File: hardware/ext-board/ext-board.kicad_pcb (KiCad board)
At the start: 2 copper layers, 38.5 x 85 mm, 13 parts, among them J1 PTSM 0,5/5-HH-2,5-THR, J2 VCC DATA GND, U1 DS2482-100, U2 DS2482-100 (0x19)

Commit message: hardware: silkscreen tidied, MOV position dropped, copper plots for the review
Plug designators sit below their pin labels (J4's beside the capacitor),
the resistor references run along their bodies, the diode references sit
at the board edge end of each diode, the link header references sit on the
rib strip beside them, the capacitor's beside its lower pad, and the empty
bottom field says why it is empty. The MOV position is gone: the strip
beside the capacitor holds the PTC and the J4 labels, and a clamp on a
class 2 transformer's 24 VAC is a nicety. GPIO8's run from header pin 24
to its breakout pad, which threads the column twice through 0.84 mm gaps,
is laid by hand because the router managed it only sometimes. EXT: C1's
reference moves below the part, clear of the H2 label.

Both boards carry front and back copper plots (back mirrored) from
kicad-cli for checking traces; the review document shows both faces of
each board and the copper.

Co-Authored-By: Claude Fable 5.1 <noreply@anthropic.com>
Claude-Session: https://claude.ai/code/session_01WPMStupqhasFMcGr3goMno
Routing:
- net DATA: track 133.3 -> 158.2 mm, vias 1 -> 0
- net SCL: track 59.8 -> 45.0 mm
- net GND: track 153.7 -> 146.6 mm
- net SDA: track 61.6 -> 56.9 mm
- net H3_DATA: track 37.2 -> 39.0 mm
- net VCC: track 109.1 -> 110.0 mm

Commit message: hardware: EXT link header against the riser field, plug access kept clear
The housing's opening to the INT board, the one the INT link headers sit
beside, falls on the right of the EXT board at the link header's height,
and the PTSM plugs come in and out through it. The power riser is unused
and the housing comes close to the board only at the lower end of its hole
field (David, 2026-09-12), so the riser rule area shrinks to columns 1-3
and J1 moves against it (body x 8.5-22.7), with U2's decoupling beside JP2
and the cleared band marked on the silkscreen.

Routed, DRC clean, schematic parity kept; Gerbers and copper plots
re-exported.

Co-Authored-By: Claude Fable 5.1 <noreply@anthropic.com>
Claude-Session: https://claude.ai/code/session_01WPMStupqhasFMcGr3goMno
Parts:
- moved C2 12.0 mm to (18.5, 34.0)
- moved J1 9.75 mm to (15.6, 44.3)
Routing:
- net VCC: track 110.0 -> 143.0 mm, vias 1 -> 0
- net DATA: track 158.2 -> 143.4 mm
- net SDA: track 56.9 -> 48.7 mm
- net H3_DATA: track 39.0 -> 31.9 mm
- net GPIO4: track 39.6 -> 44.9 mm
- net SCL: track 45.0 -> 50.3 mm, vias 0 -> 1
- net GND: track 146.6 -> 145.5 mm
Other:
- board text added: "plug access: keep clear"

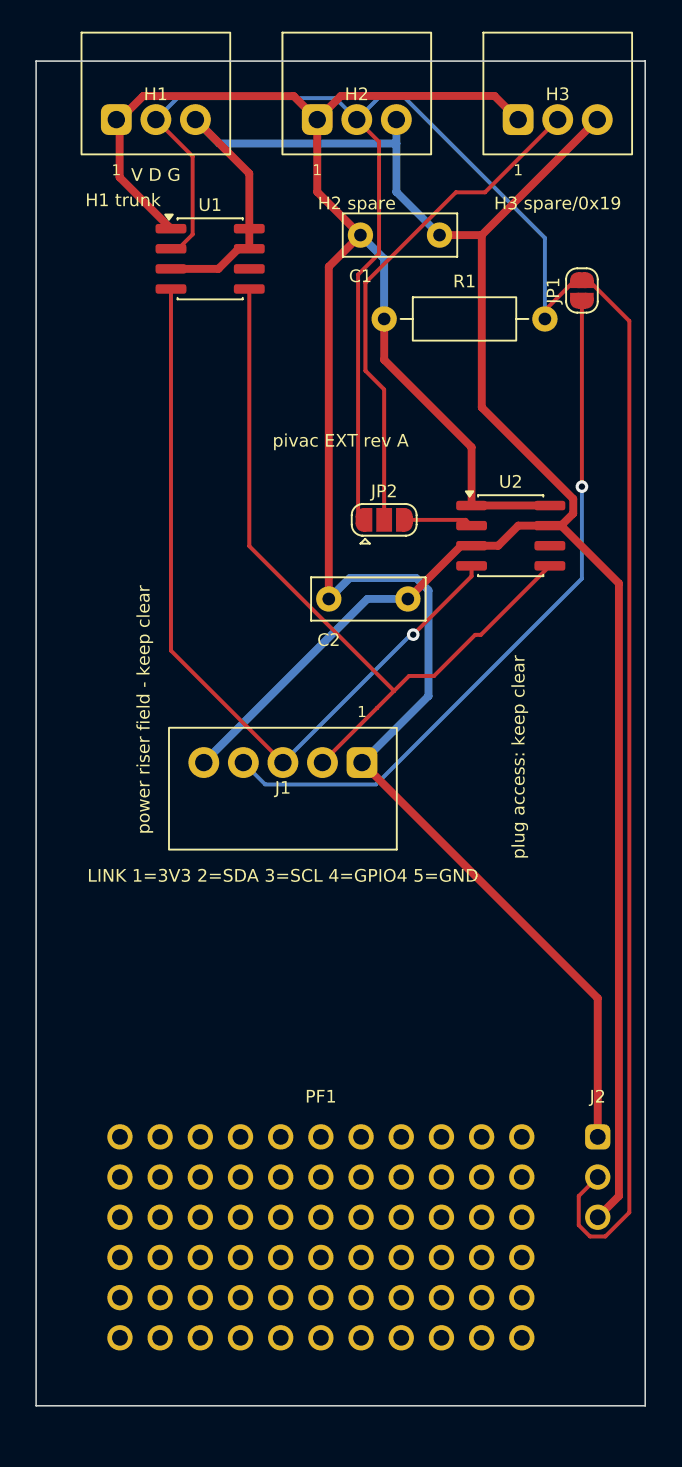
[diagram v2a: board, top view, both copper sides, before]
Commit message: Rev B plan: Pi supply on EXT, GH link, every channel on a plug (#214)
* Rev B plan: the Pi's supply moves to the EXT board, GH link, every channel on a plug

Rev A left the Pi on a wall adapter and put the 24 VAC entry on INT, which cost
two plug positions and forced HPCOOL onto the J8 pigtail whose loose connector
was the one fault at the 2026-09-26 cutover. Rev B moves the entry, the PTC, the
bridge and the reservoir to EXT's mid field, adds an isolated Traco TMR 12-4811WI
there, and feeds the Pi's own USB-C by a pigtail from a 2-pin XH header, so the
Pi's input protection stays in circuit and header pins 2 and 4 carry nothing.
VS and COM come back to INT over a 7-way JST GH link that replaces the PTSM
J6/J7 pair and latches after the boards are seated. J4 then takes HPCOOL, DHWX
and SP-E, J8 goes away, the optocoupler sockets shift right to clear the J9
breakout, and both boards get a DL title block.

The plan doc carries the circuit, the link pin map, the plug map, the EXT
positions, the parts list with distributor links and the path to the OSH Park
order. The SVG is the layout for review at 8 px per mm; hardware/dl-monogram.svg
is the mark's source for the KiCad footprint. The PCB plan's power section and
open items now state the rev B position.

Co-Authored-By: Claude Fable 5.1 <noreply@anthropic.com>

* Rev B plan: component index for both boards, PTSM edge offsets, link header at the rib

The plan now names every reference designator on both boards with its part,
body size, position and purpose, states how each PTSM header meets its board
edge (pin row 5.4 mm behind the entry face, from the Phoenix drawing the
footprint is built from: INT plugs 1.55 mm inside, EXT sockets and J3 1.7 mm
outside), and carries the carried-over parts alongside the new ones. EXT's J1
moves down to y 46.5-58.5 so it does not sit opposite INT's J6 in the opening.
The layout SVG draws the PTSM bodies at those offsets and J1 at its new place.

Co-Authored-By: Claude Fable 5.1 <norepl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
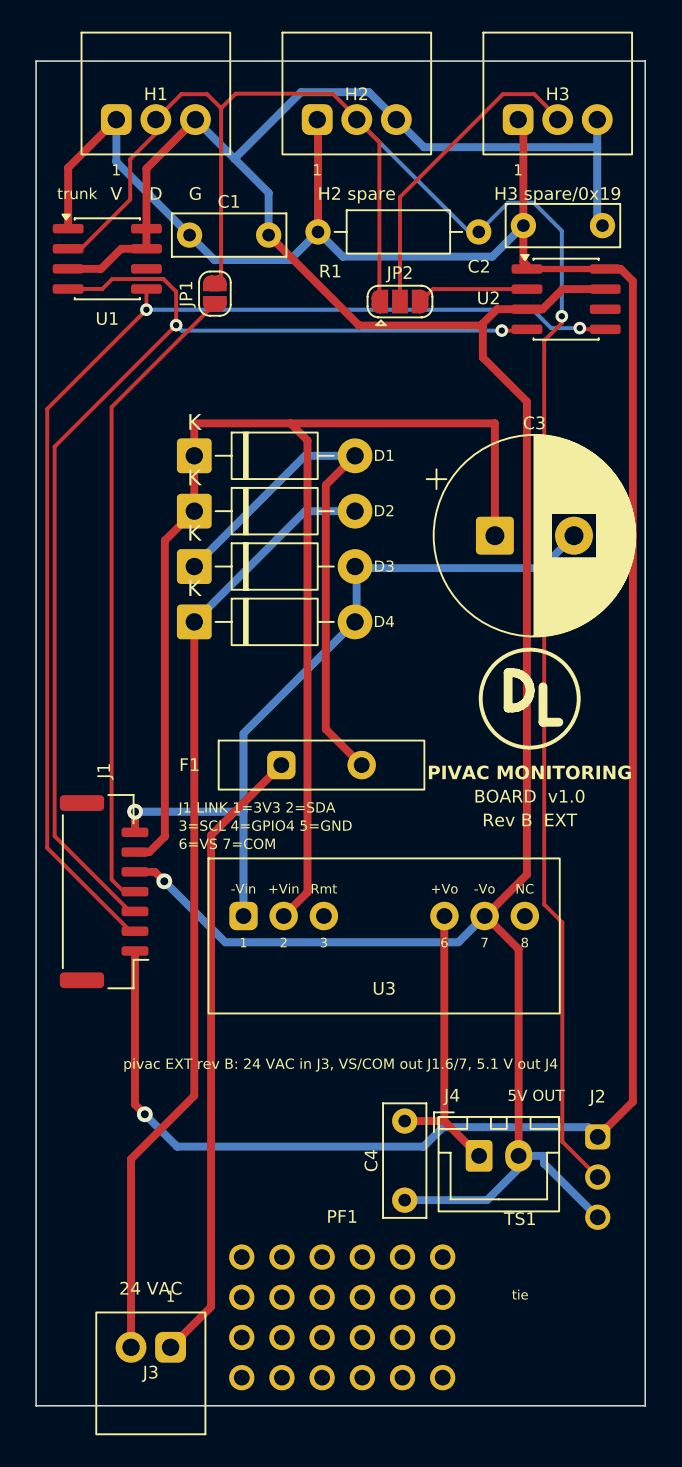
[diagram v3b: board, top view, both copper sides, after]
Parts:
- added C3: 470u 63V, CP_Radial_D12.5mm_P5.00mm, F.Cu at (29.0, 30.0)
- added C4: 1u, C_Rect_L7.0mm_W2.5mm_P5.00mm, F.Cu at (23.3, 67.0)
- added D1: 1N4007, D_DO-41_SOD81_P10.16mm_Horizontal, F.Cu at (10.0, 24.9)
- added D2: 1N4007, D_DO-41_SOD81_P10.16mm_Horizontal, F.Cu at (10.0, 28.4)
- added D3: 1N4007, D_DO-41_SOD81_P10.16mm_Horizontal, F.Cu at (10.0, 31.9)
- added D4: 1N4007, D_DO-41_SOD81_P10.16mm_Horizontal, F.Cu at (10.0, 35.5)
- added F1: PTC 1.1A 60V, pivac:PTC_Radial_P5.08_Standing, F.Cu at (18.0, 44.5)
- added J3: PTSM 0,5/2-HH-2,5-THR 24 VAC, pivac:PTSM_0.5_2-HH-2.5-THR, F.Cu at (7.25, 81.3)
- added J4: 5V OUT to Pi USB-C, JST_XH_B2B-XH-A_1x02_P2.50mm_Vertical, F.Cu at (28.0, 69.2)
- added TS1: tie slots, pivac:TieSlots_2x, F.Cu at (30.6, 75.6)
- added U3: TMR 12-4811WI, pivac:TMR12WI_SIP-8, F.Cu at (13.1, 54.0)
- J1: value PTSM 0,5/5-HH-2,5-THR -> GH BM07B link to INT; footprint pivac:PTSM_0.5_5-HH-2.5-THR -> JST_GH_BM07B-GHS-TBT_1x07-1MP_P1.25mm_Vertical
- PF1: footprint pivac:Proto_11x6 -> pivac:Proto_6x4
- moved C2 26.6 mm to (30.8, 10.4)
- moved JP1 23.2 mm to (11.3, 14.7)
- moved U2 15.4 mm to (33.5, 15.1)
- moved J1 13.9 mm to (4.30, 52.5), turned to 90 degrees
- moved JP2 13.8 mm to (23.0, 15.2)
- moved PF1 10.8 mm to (13.0, 75.6)
- moved C1 10.8 mm to (9.70, 11.0)
- moved R1 6.91 mm to (17.8, 10.8)
- moved U1 6.50 mm to (4.50, 12.5)
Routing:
- net VS: track 0.00 -> 87.5 mm
- net ACC: track 0.00 -> 60.6 mm
- net COM: track 0.00 -> 47.8 mm, vias 0 -> 1
- net ACR: track 0.00 -> 39.7 mm
- net ACF: track 0.00 -> 34.3 mm
- net GND: track 145.5 -> 178.1 mm, vias 0 -> 1
- net SDA: track 48.7 -> 75.2 mm, vias 0 -> 2
- net SCL: track 50.3 -> 74.4 mm, vias 1 -> 2
- net +5V: track 0.00 -> 18.6 mm
- net VCC: track 143.0 -> 161.0 mm, vias 0 -> 1
- net DATA: track 143.4 -> 128.2 mm, vias 0 -> 1
- net H3_DATA: track 31.9 -> 20.0 mm
- net GPIO4: track 44.9 -> 40.9 mm, vias 1 -> 0
- net DATA_H3: track 4.38 -> 7.05 mm
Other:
- board text added: "24 VAC"
- board text added: "3=SCL 4=GPIO4 5=GND"
- board text added: "5V OUT"
- board text added: "6=VS 7=COM"
- board text added: "BOARD v1.0"
- board text added: "D"
- board text added: "G"
- board text added: "J1 LINK 1=3V3 2=SDA"
- board text added: "PIVAC MONITORING"
- board text added: "Rev B EXT"
- board text added: "V"
- board text added: "pivac EXT rev B: 24 VAC in J3, VS/COM out J1.6/7, 5.1 V out J4"
- board text added: "trunk"
- board text removed: "H1 trunk"
- board text removed: "LINK 1=3V3 2=SDA 3=SCL 4=GPIO4 5=GND"
- board text removed: "V D G"
- board text removed: "pivac EXT rev A"
- board text removed: "plug access: keep clear"
- board text removed: "power riser field - keep clear"
